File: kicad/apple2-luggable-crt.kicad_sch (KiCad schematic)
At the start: 233 parts, among them J1 VIDEO IN, J401 DEFLECTION YOKE, J402 CRT SOCKET BRD, J501 CRT SOCKET BRD, J801 12V UNREG, K6 Jumper_2_Bridged, K9+ Jumper_2_Bridged, K9- Jumper_2_Bridged, Q201 2SA562Y, Q202 2SC1815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

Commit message: compress the schematic layout somewhat
- page size is currently A4.  I think I can get it down to A3 if I squeeze things around.  we'll see.
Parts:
- R209, R225, R419: Comment * -> (none)
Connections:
- net -Y: now reaches Q501.23 (-Y_OUT), R221.1
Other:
- moved on the sheet: C1, C202, C203, C204, C205, C206, C207, C208, C209, C210, C301, C302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

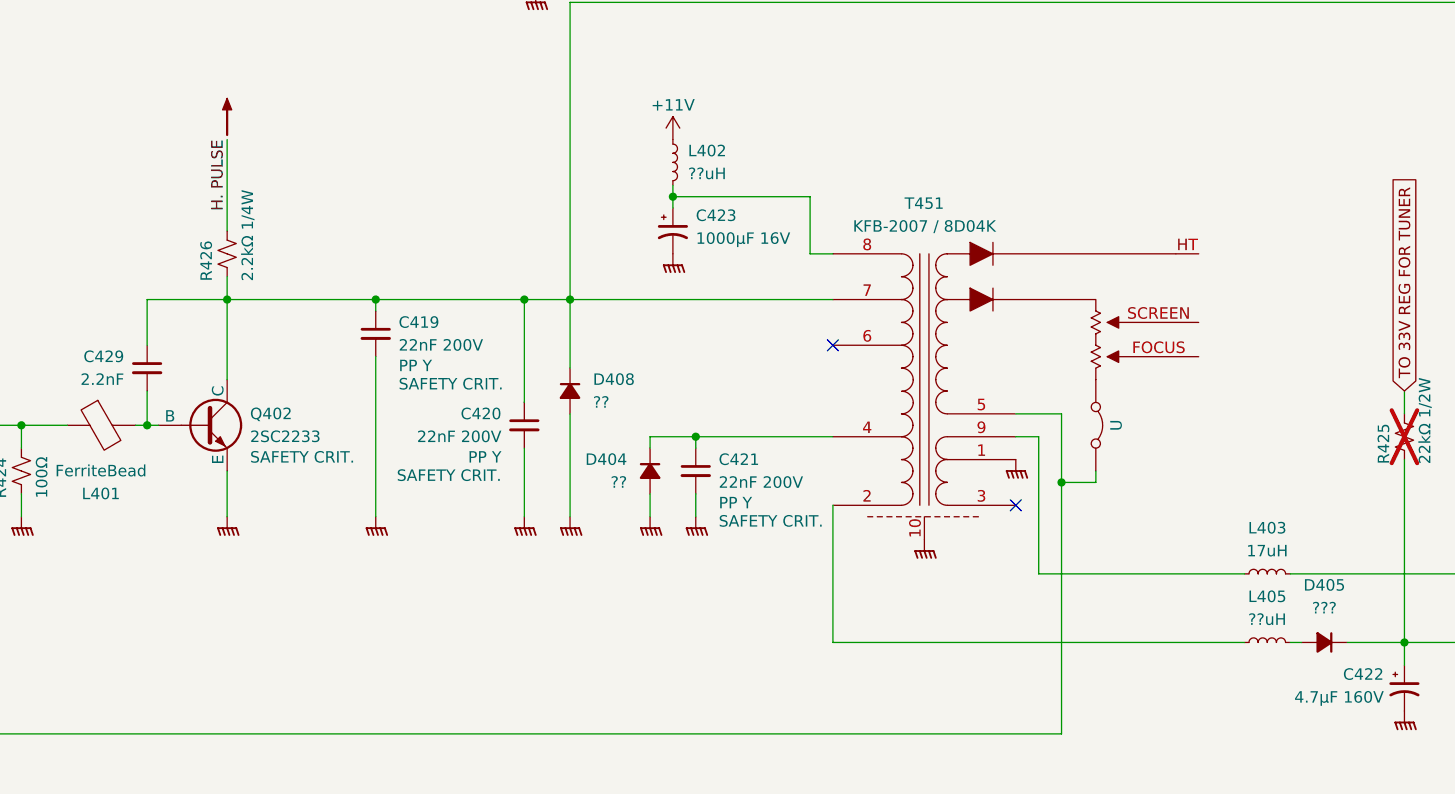
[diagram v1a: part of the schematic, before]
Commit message: start assigning footprints
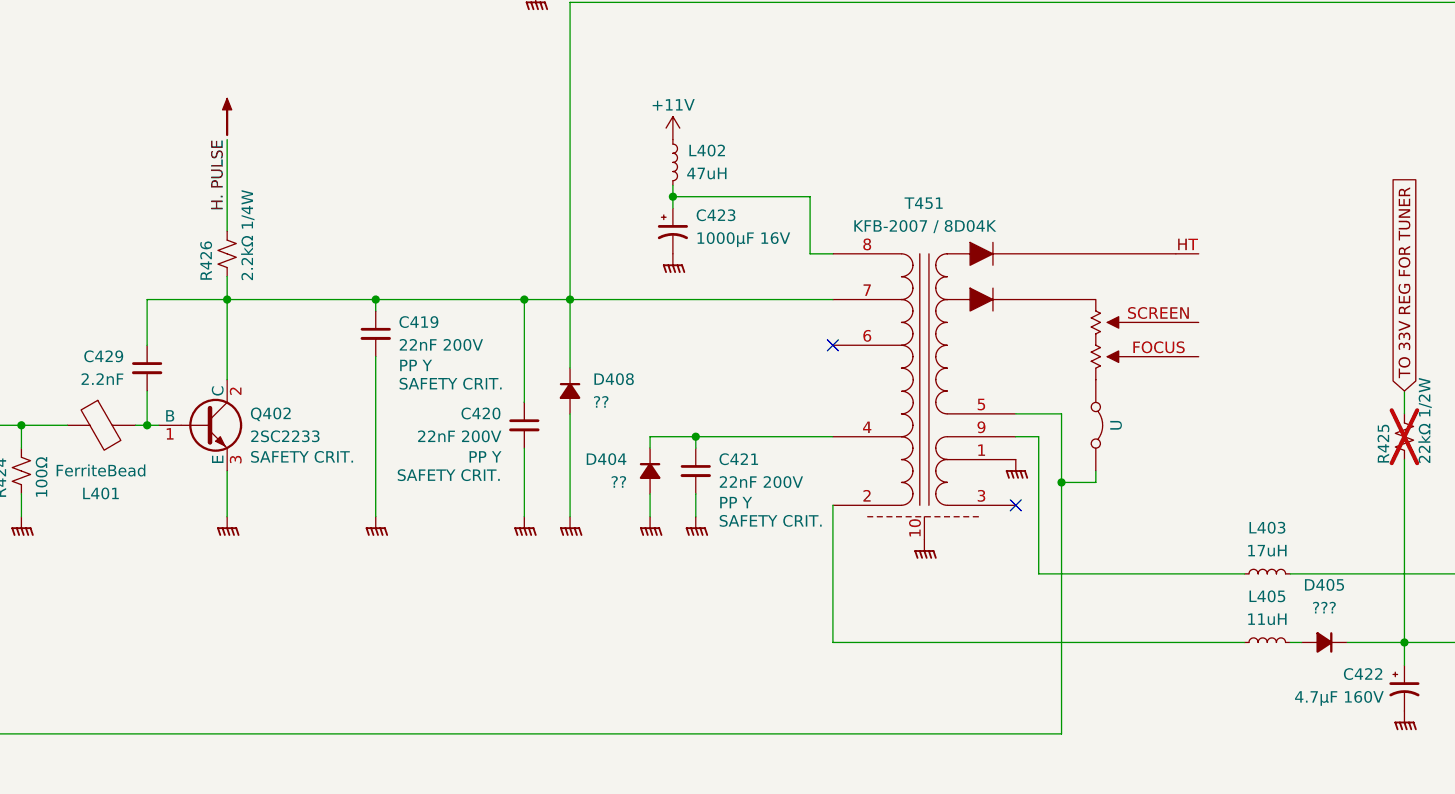
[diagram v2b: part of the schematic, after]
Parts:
- C551: footprint (none) -> Capacitor_THT:C_Rect_L7.0mm_W6.5mm_P5.00mm
- J801: footprint (none) -> Connector_BarrelJack:BarrelJack_Wuerth_6941xx301002
- L402: value ??uH -> 47uH; footprint (none) -> Inductor_THT:L_Radial_D7.8mm_P5.00mm_Fastron_07HCP
- L405: value ??uH -> 11uH; footprint (none) -> foodprints:L_Radial_D10.0mm_P7.62mm
- Q402: footprint (none) -> Package_TO_SOT_THT:TO-220-3_Vertical; symbol Simulation_SPICE:NPN -> Transistor_BJT:Q_NPN_BCE
- R201, R314, R320, R418: footprint (none) -> Resistor_THT:R_Axial_DIN0207_L6.3mm_D2.5mm_P15.24mm_Horizontal
- X501: footprint (none) -> Crystal:Crystal_HC49-U_Vertical
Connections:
- net at C429.2, L401.2: now also Q402.1 (B); no longer Q402.2 (B)
- net at C419.1, C420.1, C429.1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: now also Q402.2 (C); no longer Q402.1 (C)
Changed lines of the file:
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@@
 			)
 		)
-		(property "Value" "??uH"
+		(property "Value" "47uH"
 			(at 372.11 226.06 0)
 			(effects
@@
 			)
 		)
-		(property "Footprint" ""
+		(property "Footprint" "Inductor_THT:L_Radial_D7.8mm_P5.00mm_Fastron_07HCP"
 			(at 368.3 224.79 0)
 			(effects
@@
 			)
 		)
-		(property "Footprint" ""
+		(property "Footprint" "Crystal:Crystal_HC49-U_Vertical"
 			(at 302.26 179.07 0)
 			(effects
@@
 			)
 		)
-		(property "Footprint" ""
+		(property "Footprint" "Resistor_THT:R_Axial_DIN0207_L6.3mm_D2.5mm_P15.24mm_Horizontal"
 			(at 353.06 195.58 0)
 			(effects
@@
 			)
 		)
-		(property "Footprint" ""
+		(property "Footprint" "Resistor_THT:R_Axial_DIN0207_L6.3mm_D2.5mm_P15.24mm_Horizontal"
 			(at 35.56 64.77 0)
 			(effects
@@
 			)
 		)
-		(property "Footprint" ""
+		(property "Footprint" "Connector_BarrelJack:BarrelJack_Wuerth_6941xx301002"
 			(at 26.67 31.496 0)
 			(effects
@@
 	)
 	(symbol
-		(lib_id "Simulation_SPICE:NPN")
+		(lib_id "Transistor_BJT:Q_NPN_BCE")
 		(at 316.23 254 0)
 		(unit 1)
@@
 			)
 		)
-		(property "Footprint" ""
-			(at 379.73 254 0)
+		(property "Footprint" "Package_TO_SOT_THT:TO-220-3_Vertical"
+			(at 321.31 251.46 0)
 			(effects
 				(font
@@
 			)
 		)
-		(property "Datasheet" "https://ngspice.sourceforge.io/docs/ngspice-html-manual/manual.xhtml#cha_BJTs"
-			(at 379.73 254 0)
+		(property "Datasheet" "~"
+			(at 316.23 254 0)
 			(effects
 				(font
@@
 			)
 		)
-		(property "Description" "Bipolar transistor symbol for simulation only, substrate tied to the emitter"
+		(property "Description" "NPN transistor, base/collector/emitter"
 			(at 316.23 254 0)
 			(effects
@@
 			)
 		)
-		(property "Sim.Pins" "1=C 2=B 3=E"
+		(property "Sim.Pins" "1=B 2=C 3=E"
 			(at 316.23 254 0)
 			(effects
@@
 			)
 		)
-		(property "Value" "??uH"
+		(property "Value" "11uH"
 			(at 434.34 275.59 90)
 			(effects
@@
 			)
 		)
-		(property "Footprint" ""
+		(property "Footprint" "foodprints:L_Radial_D10.0mm_P7.62mm"
 			(at 434.34 278.13 0)
 			(effects
@@
 			)
 		)
-		(property "Footprint" ""
+		(property "Footprint" "Resistor_THT:R_Axial_DIN0207_L6.3mm_D2.5mm_P15.24mm_Horizontal"
 			(at 447.04 167.64 0)
 			(effects
@@
 			)
 		)
-		(property "Footprint" ""
+		(property "Footprint" "Capacitor_THT:C_Rect_L7.0mm_W6.5mm_P5.00mm"
 			(at 297.18 190.5 0)
 			(effects
@@
 			)
 		)
-		(property "Footprint" ""
+		(property "Footprint" "Resistor_THT:R_Axial_DIN0207_L6.3mm_D2.5mm_P15.24mm_Horizontal"
 			(at 448.31 123.19 0)
 			(effects

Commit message: more work on foot prints
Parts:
- DL201: footprint (none) -> foodprints:DelayLine_Sangshin_DL601T
- L403: footprint (none) -> foodprints:L_Radial_D6.0mm_P8.00mm
- L405: value 11uH -> 10uH
- L410: value ??uH -> 2uH; footprint (none) -> Inductor_THT:L_Radial_D7.5mm_P5.00mm_Fastron_07P
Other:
- moved on the sheet: C205, C209, C210, C311, DL201, J401, L201, Q202, Q303, Q304, R207, R208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

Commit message: more progress
- more foot prints
- fixed some errors (there was an inductor I had missed altogether)
- figured out all the inductor values
- figured out, more or less, most of the diodes
- rearranged things to squeeze it onto an A3 sheet.  when printed onto A4, the components are more compactly arranged but individually larger, and the component values are easier to read.
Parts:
- removed L301, L408, L501: ??uH, symbol Device:L_Small
- added L301: 1mH, Inductor_THT:L_Radial_D7.5mm_P5.00mm_Fastron_07P, symbol Device:L_Ferrite
- added L407: 2.1μH, Inductor_THT:L_Radial_D7.5mm_P5.00mm_Fastron_07P, symbol Device:L_Ferrite
- added L408: 150μH, Inductor_THT:L_Radial_D7.5mm_P5.00mm_Fastron_07P, symbol Device:L_Ferrite
- added L409: FerriteBead, foodprints:Ferrite_L12.0mm_D3.2mm_P18.0mm_Horizontal, symbol Device:FerriteBead
- added L501: 18μH, Inductor_THT:L_Radial_D7.5mm_P5.00mm_Fastron_07P, symbol Device:L_Ferrite
- C420: value 22nF 200V -> 10nF 200V
- C421: value 22nF 200V -> 27nF 200V
- D303: value 1SR35-100A -> 1SR35-100A (??)
- D402: Comment values are for CX60, check -> marked "48T" or cyclic perm. maybe 1N4148?
- D404: value ?? -> TVR06D
- D408: value ?? -> RGP10G
- DL201: value DelayLine -> Sangshin DL601T
- L401: footprint (none) -> foodprints:Ferrite_L12.0mm_D3.2mm_P18.0mm_Horizontal
- L402: value 47uH -> 47μH; symbol Device:L_Small -> Device:L_Ferrite
- L403: value 17uH -> 17μH; symbol Device:L_Small -> Device:L_Ferrite
- L405: value KLN 2028 (?) -> 10μH; symbol Device:L_Iron -> Device:L_Ferrite
- L406: renamed from L405; value 10uH -> 200μH; footprint foodprints:L_Radial_D10.0mm_P7.62mm -> Inductor_THT:L_Radial_D7.5mm_P5.00mm_Fastron_07P; symbol Device:L_Small -> Device:L_Ferrite
- L410: value 2uH -> 1μH; symbol Device:L_Small -> Device:L_Ferrite
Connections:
- net GNDPWR: now also L409.2, L501.1; no longer Q402.3 (E)
- net at C301.1, R301.2, R302.1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: now also L301.2
- net at C413.1, C434.2, Q501.32 (H_DRIVE_OUT): now also L407.2; no longer R413.1, R416.1
- net at Q501.36 (SYNC_SEP._OUT), R304.1: now also L301.1
- net at C519.1, R501.1, R535.2: now also L501.2
- net at R401.1: now also L408.1
- net at C402.2, D401.1 (K): now also L408.2
- new net: L407.1, R413.1, R416.1
- new net: L409.1, Q402.3 (E)
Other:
- moved on the sheet: C1, C201, C202, C203, C204, C205, C206, C207, C208, C209, C210, C301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

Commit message: more progress
- more foot prints
- fix one of the diodes (turns out not to be a zener)
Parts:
- D402: value MA4075(M) -> (none); symbol Device:D_Zener_Small_Filled -> Device:D_Small_Filled; Comment marked "48T" or cyclic perm. maybe 1N4148? -> (none)
- SW201: footprint (none) -> foodprints:SW_SERVICE
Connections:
- net at C301.1, L301.2, R301.2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: now also R304.1; no longer R304.2
- net at L301.1, Q501.36 (SYNC_SEP._OUT): now also R304.2; no longer R304.1
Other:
- note added: "RESISTOR WAS BOARD MOD"
- moved on the sheet: C203, C209, C210, C304, C406, C407, C412, C427, C428, C435, C505, C506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

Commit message: more progress
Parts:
- D402: value (none) -> ~
- T401: footprint (none) -> foodprints:Transformer_Horiz_Drive; symbol Device:L_Ferrite_Coupled_1243 -> Transformer:ZMPT101K
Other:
- title: (none) -> SKYTEK SCT-1024
- moved on the sheet: C1, C205, C412, C418, C419, C420, C426, C427, C428, C429, C506, D404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

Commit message: more progress
- add notes about inductors
- label the orientations of most variable resistors
- fix a few other issues here and there
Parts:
- renumbered R307 to R351
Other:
- moved on the sheet: R354
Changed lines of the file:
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@@
 		)
 	)
+	(text_box "CW"
+		(exclude_from_sim no)
+		(at 146.05 34.29 0)
+		(size 3.81 2.54)
+		(margins 0.9525 0.9525 0.9525 0.9525)
+		(stroke
+			(width 0)
+			(type solid)
+		)
+		(fill
+			(type none)
+		)
+		(effects
+			(font
+				(size 1.016 1.016)
+			)
+		)
+	)
 	(text_box "SUB BRIGHT"
 		(exclude_from_sim no)
@@
 		)
 	)
+	(text_box "CCW"
+		(exclude_from_sim no)
+		(at 58.42 241.3 0)
+		(size 3.81 2.54)
+		(margins 0.9525 0.9525 0.9525 0.9525)
+		(stroke
+			(width 0)
+			(type solid)
+		)
+		(fill
+			(type none)
+		)
+		(effects
+			(font
+				(size 1.016 1.016)
+			)
+		)
+	)
+	(text_box "CCW"
+		(exclude_from_sim no)
+		(at 30.48 209.55 0)
+		(size 3.81 2.54)
+		(margins 0.9525 0.9525 0.9525 0.9525)
+		(stroke
+			(width 0)
+			(type solid)
+		)
+		(fill
+			(type none)
+		)
+		(effects
+			(font
+				(size 1.016 1.016)
+			)
+		)
+	)
 	(text_box "TINT"
 		(exclude_from_sim no)
@@
 		)
 	)
+	(text_box "CW"
+		(exclude_from_sim no)
+		(at 99.06 189.23 0)
+		(size 3.81 2.54)
+		(margins 0.9525 0.9525 0.9525 0.9525)
+		(stroke
+			(width 0)
+			(type solid)
+		)
+		(fill
+			(type none)
+		)
+		(effects
+			(font
+				(size 1.016 1.016)
+			)
+		)
+	)
+	(text_box "CW"
+		(exclude_from_sim no)
+		(at 179.07 54.61 0)
+		(size 3.81 2.54)
+		(margins 0.9525 0.9525 0.9525 0.9525)
+		(stroke
+			(width 0)
+			(type solid)
+		)
+		(fill
+			(type none)
+		)
+		(effects
+			(font
+				(size 1.016 1.016)
+			)
+		)
+	)
+	(text_box "CW"
+		(exclude_from_sim no)
+		(at 299.72 166.37 0)
+		(size 3.81 2.54)
+		(margins 0.9525 0.9525 0.9525 0.9525)
+		(stroke
+			(width 0)
+			(type solid)
+		)
+		(fill
+			(type none)
+		)
+		(effects
+			(font
+				(size 1.016 1.016)
+			)
+		)
+	)
 	(text_box "8.6V"
 		(exclude_from_sim no)
@@
 		)
 	)
+	(text_box "CW"
+		(exclude_from_sim no)
+		(at 151.13 187.96 0)
+		(size 3.81 2.54)
+		(margins 0.9525 0.9525 0.9525 0.9525)
+		(stroke
+			(width 0)
+			(type solid)
+		)
+		(fill
+			(type none)
+		)
+		(effects
+			(font
+				(size 1.016 1.016)
+			)
+		)
+	)
 	(text_box "HEATER ACV"
 		(exclude_from_sim no)
@@
 		)
 	)
+	(text_box "CW"
+		(exclude_from_sim no)
+		(at 50.8 256.54 0)
+		(size 3.81 2.54)
+		(margins 0.9525 0.9525 0.9525 0.9525)
+		(stroke
+			(width 0)
+			(type solid)
+		)
+		(fill
+			(type none)
+		)
+		(effects
+			(font
+				(size 1.016 1.016)
+			)
+		)
+	)
 	(junction
 		(at 257.81 31.75)
@@
 	)
 	(junction
+		(at 312.42 165.1)
+		(diameter 0)
+		(color 0 0 0 0)
+	)
+	(junction
 		(at 185.42 48.26)
 		(diameter 0)
@@
 	)
 	(junction
-		(at 308.61 165.1)
-		(diameter 0)
-		(color 0 0 0 0)
-	)
-	(junction
 		(at 139.7 40.64)
 		(diameter 0)
@@
 	(wire
 		(pts
-			(xy 302.26 165.1) (xy 308.61 165.1)
+			(xy 302.26 165.1) (xy 312.42 165.1)
 		)
 		(stroke
@@
 	(wire
 		(pts
-			(xy 59.69 53.34) (xy 62.23 53.34)
+			(xy 312.42 165.1) (xy 314.96 165.1)
 		)
 		(stroke
@@
 	(wire
 		(pts
-			(xy 281.94 73.66) (xy 281.94 72.39)
+			(xy 59.69 53.34) (xy 62.23 53.34)
 		)
 		(stroke
@@
 	(wire
 		(pts
-			(xy 175.26 223.52) (xy 175.26 229.87)
+			(xy 281.94 73.66) (xy 281.94 72.39)
 		)
 		(stroke
@@
 	(wire
 		(pts
-			(xy 200.66 214.63) (xy 200.66 218.44)
+			(xy 175.26 223.52) (xy 175.26 229.87)
 		)
 		(stroke
@@
 	(wire
 		(pts
-			(xy 256.54 91.44) (xy 262.89 91.44)
+			(xy 200.66 214.63) (xy 200.66 218.44)
 		)
 		(stroke
@@
 	(wire
 		(pts
-			(xy 308.61 165.1) (xy 314.96 165.1)
+			(xy 256.54 91.44) (xy 262.89 91.44)
 		)
 		(stroke
@@
 	(wire
 		(pts
-			(xy 308.61 165.1) (xy 308.61 166.37)
+			(xy 312.42 165.1) (xy 312.42 166.37)
 		)
 		(stroke
@@
 	(symbol
 		(lib_id "Device:R_Small_US")
-		(at 308.61 168.91 0)
+		(at 312.42 168.91 0)
 		(unit 1)
 		(exclude_from_sim no)
@@
 		(dnp no)
 		(property "Reference" "R354"
-			(at 307.086 168.148 0)
+			(at 310.896 168.148 0)
 			(effects
 				(font
@@
 		)
 		(property "Value" "1kΩ"
-			(at 307.086 170.18 0)
+			(at 310.896 170.18 0)
 			(effects
 				(font
@@
 		)
 		(property "Footprint" ""
-			(at 308.61 168.91 0)
+			(at 312.42 168.91 0)
 			(effects
 				(font
@@
 		)
 		(property "Datasheet" "~"
-			(at 308.61 168.91 0)
+			(at 312.42 168.91 0)
 			(effects
 				(font
@@
 		)
 		(property "Description" "Resistor, small US symbol"
-			(at 308.61 168.91 0)
+			(at 312.42 168.91 0)
 			(effects
 				(font
@@
 		(dnp no)
 		(property "Reference" "R555"
-			(at 103.632 191.77 0)
+			(at 103.632 193.04 0)
 			(effects
 				(font
@@
 		)
 		(property "Value" "10kΩ B"
-			(at 103.632 194.056 0)
+			(at 103.632 195.072 0)
 			(effects
 				(font
@@
 		(on_board yes)
 		(dnp no)
-		(property "Reference" "R307"
+		(property "Reference" "R351"
 			(at 187.198 52.07 0)
 			(effects
@@
 			(project "apple2-luggable-crt"
 				(path "/b139b959-2b3e-49ad-9a77-d02564fe1a08"
-					(reference "R307")
+					(reference "R351")
 					(unit 1)
 				)
@@
 	(symbol
 		(lib_id "power:GNDPWR")
-		(at 308.61 171.45 0)
+		(at 312.42 171.45 0)
 		(mirror y)
 		(unit 1)
@@
 		(dnp no)
 		(property "Reference" "#PWR083"
-			(at 308.61 176.53 0)
+			(at 312.42 176.53 0)
 			(effects
 				(font
@@
 		)
 		(property "Value" "GNDPWR"
-			(at 308.737 175.26 0)
+			(at 312.547 175.26 0)
 			(effects
 				(font
@@
 		)
 		(property "Footprint" ""
-			(at 308.61 172.72 0)
+			(at 312.42 172.72 0)
 			(effects
 				(font
@@
 		)
 		(property "Datasheet" ""
-			(at 308.61 172.72 0)
+			(at 312.42 172.72 0)
 			(effects
 				(font
@@
 		)
 		(property "Description" "Power symbol creates a global label with name \"GNDPWR\" , global ground"
-			(at 308.61 171.45 0)
+			(at 312.42 171.45 0)
 			(effects
 				(font

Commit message: more progress
- completed confirming all components out of circuit
- fixed several errors and omissions
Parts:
- removed C210: 22pF, symbol Device:C_Small
- removed L201: 47, symbol Device:L_Small
- added C210: 1000μF 16V, symbol Device:C_Polarized_Small_US
- added C502: 2.2nF, symbol Device:C_Small
- added C803: 330μF 16V, symbol Device:C_Polarized_Small_US
- C206: value 33μF 16V -> 47nF; symbol Device:C_Polarized_Small_US -> Device:C_Small; now fitted
- C511: value 12pF -> 7pF
- C514, C515: value 22nF -> 22nF 100V
- D203, D301, D302, D401, D403: value 1SS133 -> 1N4148
- D402: value ~ -> 1N4148
- Q201: value 2SA562Y -> 2SA562-Y
- Q202: value 2SC1815 -> 2SC1815-Y
- Q401: value 2SC200Y -> 2SC200-Y
- R221: value 330kΩ -> 330Ω
- R222: value 680Ω -> 300Ω
- R229: value 220Ω -> 1.1kΩ
- R321: value 160Ω -> 160Ω 1/2 W
- R323: value 310Ω 1/2W -> 300Ω 1/2W
- R405: value 110kΩ -> 220kΩ
- R409: value 22kΩ -> 39kΩ
- renumbered C1 to C417
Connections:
- net +10V: now also C210.1
- net +11V: now also C803.1
- net CHROMA: now also C502.1; no longer R501.2, R502.1
- net GNDPWR: now also C210.2, C803.2
- new net: C502.2, R501.2, R502.1
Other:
- moved on the sheet: C201, C202, C203, C204, C205, C207, C208, C209, C301, C302, C303, C304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
